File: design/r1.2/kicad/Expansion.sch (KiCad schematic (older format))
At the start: 27 parts, among them IC1 MC68010P10, IC4 MC68901P, IC6 74174N, IC9 74LS01N, J1 PWR, J3 Conn_02x32_Odd_Even, J5 GPIO-PANEL

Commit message: Layout for 1.2 and PLD changes for same
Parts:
- J5: symbol Connector_Generic:Conn_2Rows-15Pins -> Connector_Generic:Conn_02x08_Odd_Even
- renumbered C13 to C14, C14 to C15, C15 to C16, C16 to C17, C17 to C18, C23 to C19, C18 to C20, C25 to C21, C19 to C22, C20 to C23, C21 to C24, C22 to C25, C24 to C26, R15 to R17, R16 to R18, R17 to R19
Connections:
- net GND: now also J5.16 (Pin_16)
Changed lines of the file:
@@
 $EndComp
 $Comp
-L Connector_Generic:Conn_2Rows-15Pins J5
+L Connector_Generic:Conn_02x08_Odd_Even J5
 U 1 1 600521A7
 P 10250 7000
@@
 Text GLabel 10050 7400 0    50   Input ~ 0
 TAI
-Text GLabel 10550 7300 2    50   Input ~ 0
-TBI
 Text GLabel 11300 2800 2    50   Input ~ 0
 VPA
@@
 	10300 8100 10300 7950
 $Comp
-L Device:R R17
+L Device:R R19
 U 1 1 600B8632
 P 11100 2300
-F 0 "R17" H 11170 2346 50  0000 L CNN
+F 0 "R19" H 11170 2346 50  0000 L CNN
 F 1 "10K" H 11170 2255 50  0000 L CNN
 F 2 "rosco_m68k:0207_10" V 11030 2300 50  0001 C CNN
@@
 AR Path="/5F55DF35" Ref="C?"  Part="1"
 AR Path="/5E53B952/5F55DF35" Ref="C?"  Part="1"
-AR Path="/5E53BC83/5F55DF35" Ref="C25"  Part="1"
-F 0 "C25" H 3795 6569 59  0000 L BNN
+AR Path="/5E53BC83/5F55DF35" Ref="C21"  Part="1"
+F 0 "C21" H 3795 6569 59  0000 L BNN
 F 1 "470uF" H 3795 6369 59  0000 L BNN
 F 2 "rosco_m68k:E3,5-10" H 3750 6550 50  0001 C CNN
@@
 AR Path="/5F55DF3B" Ref="C?"  Part="1"
 AR Path="/5E53B952/5F55DF3B" Ref="C?"  Part="1"
-AR Path="/5E53BC83/5F55DF3B" Ref="C23"  Part="1"
-F 0 "C23" H 3295 6569 59  0000 L BNN
+AR Path="/5E53BC83/5F55DF3B" Ref="C19"  Part="1"
+F 0 "C19" H 3295 6569 59  0000 L BNN
 F 1 "100uF" H 3295 6369 59  0000 L BNN
 F 2 "rosco_m68k:E2,5-5" H 3250 6550 50  0001 C CNN
@@
 	11700 2700 11700 5550
 $Comp
-L Device:R R16
+L Device:R R18
 U 1 1 6009E518
 P 10550 7700
-F 0 "R16" H 10620 7746 50  0000 L CNN
+F 0 "R18" H 10620 7746 50  0000 L CNN
 F 1 "4K7" H 10620 7655 50  0000 L CNN
 F 2 "rosco_m68k:0207_10" V 10480 7700 50  0001 C CNN
@@
 $EndComp
 $Comp
-L Device:R R15
+L Device:R R17
 U 1 1 6009D68E
 P 10050 7700
-F 0 "R15" H 10120 7746 50  0000 L CNN
+F 0 "R17" H 10120 7746 50  0000 L CNN
 F 1 "4K7" H 10120 7655 50  0000 L CNN
 F 2 "rosco_m68k:0207_10" V 9980 7700 50  0001 C CNN
@@
 Wire Wire Line
 	10050 7400 10050 7550
-Wire Wire Line
-	10550 7300 10550 7550
 Wire Wire Line
 	10050 7850 10050 7950
@@
 AR Path="/5E53B630/5F6756E5" Ref="C?"  Part="1"
 AR Path="/5E53B4B8/5F6756E5" Ref="C?"  Part="1"
-AR Path="/5E53BC83/5F6756E5" Ref="C20"  Part="1"
-F 0 "C20" H 4660 8715 59  0000 L BNN
+AR Path="/5E53BC83/5F6756E5" Ref="C23"  Part="1"
+F 0 "C23" H 4660 8715 59  0000 L BNN
 F 1 "100nF" H 4660 8515 59  0000 L BNN
 F 2 "rosco_m68k:C2.5-3" H 4600 8700 50  0001 C CNN
@@
 AR Path="/5E53B630/5F6756EB" Ref="C?"  Part="1"
 AR Path="/5E53B4B8/5F6756EB" Ref="C?"  Part="1"
-AR Path="/5E53BC83/5F6756EB" Ref="C21"  Part="1"
-F 0 "C21" H 5510 8715 59  0000 L BNN
+AR Path="/5E53BC83/5F6756EB" Ref="C24"  Part="1"
+F 0 "C24" H 5510 8715 59  0000 L BNN
 F 1 "100nF" H 5510 8515 59  0000 L BNN
 F 2 "rosco_m68k:C2.5-3" H 5450 8700 50  0001 C CNN
@@
 AR Path="/5F699F50" Ref="C?"  Part="1"
 AR Path="/5E53B4B8/5F699F50" Ref="C?"  Part="1"
-AR Path="/5E53BC83/5F699F50" Ref="C18"  Part="1"
-F 0 "C18" H 3360 8715 59  0000 L BNN
+AR Path="/5E53BC83/5F699F50" Ref="C20"  Part="1"
+F 0 "C20" H 3360 8715 59  0000 L BNN
 F 1 "100nF" H 3360 8515 59  0000 L BNN
 F 2 "rosco_m68k:C2.5-3" H 3300 8700 50  0001 C CNN
@@
 AR Path="/5F699F56" Ref="C?"  Part="1"
 AR Path="/5E53B4B8/5F699F56" Ref="C?"  Part="1"
-AR Path="/5E53BC83/5F699F56" Ref="C19"  Part="1"
-F 0 "C19" H 4210 8715 59  0000 L BNN
+AR Path="/5E53BC83/5F699F56" Ref="C22"  Part="1"
+F 0 "C22" H 4210 8715 59  0000 L BNN
 F 1 "100nF" H 4210 8515 59  0000 L BNN
 F 2 "rosco_m68k:C2.5-3" H 4150 8700 50  0001 C CNN
@@
 AR Path="/5F699F5C" Ref="C?"  Part="1"
 AR Path="/5E53B4B8/5F699F5C" Ref="C?"  Part="1"
-AR Path="/5E53BC83/5F699F5C" Ref="C13"  Part="1"
-F 0 "C13" H 1195 8719 59  0000 L BNN
+AR Path="/5E53BC83/5F699F5C" Ref="C14"  Part="1"
+F 0 "C14" H 1195 8719 59  0000 L BNN
 F 1 "100uF" H 1195 8519 59  0000 L BNN
 F 2 "rosco_m68k:E2,5-5" H 1150 8700 50  0001 C CNN
@@
 AR Path="/5F699F62" Ref="C?"  Part="1"
 AR Path="/5E53B4B8/5F699F62" Ref="C?"  Part="1"
-AR Path="/5E53BC83/5F699F62" Ref="C17"  Part="1"
-F 0 "C17" H 2895 8719 59  0000 L BNN
+AR Path="/5E53BC83/5F699F62" Ref="C18"  Part="1"
+F 0 "C18" H 2895 8719 59  0000 L BNN
 F 1 "100uF" H 2895 8519 59  0000 L BNN
 F 2 "rosco_m68k:E2,5-5" H 2850 8700 50  0001 C CNN
@@
 AR Path="/5F6CD656" Ref="C?"  Part="1"
 AR Path="/5E53B952/5F6CD656" Ref="C?"  Part="1"
-AR Path="/5E53BC83/5F6CD656" Ref="C24"  Part="1"
-F 0 "C24" H 6760 8715 59  0000 L BNN
+AR Path="/5E53BC83/5F6CD656" Ref="C26"  Part="1"
+F 0 "C26" H 6760 8715 59  0000 L BNN
 F 1 "100nF" H 6760 8515 59  0000 L BNN
 F 2 "rosco_m68k:C2.5-3" H 6700 8700 50  0001 C CNN
@@
 AR Path="/5E53B810/5F6CD66A" Ref="C?"  Part="1"
 AR Path="/5E53B952/5F6CD66A" Ref="C?"  Part="1"
-AR Path="/5E53BC83/5F6CD66A" Ref="C22"  Part="1"
-F 0 "C22" H 5960 8715 59  0000 L BNN
+AR Path="/5E53BC83/5F6CD66A" Ref="C25"  Part="1"
+F 0 "C25" H 5960 8715 59  0000 L BNN
 F 1 "100nF" H 5960 8515 59  0000 L BNN
 F 2 "rosco_m68k:C2.5-3" H 5900 8700 50  0001 C CNN
@@
 AR Path="/5E53B810/5F6CD670" Ref="C?"  Part="1"
 AR Path="/5E53B952/5F6CD670" Ref="C?"  Part="1"
-AR Path="/5E53BC83/5F6CD670" Ref="C14"  Part="1"
-F 0 "C14" H 1595 8719 59  0000 L BNN
+AR Path="/5E53BC83/5F6CD670" Ref="C15"  Part="1"
+F 0 "C15" H 1595 8719 59  0000 L BNN
 F 1 "100uF" H 1595 8519 59  0000 L BNN
 F 2 "rosco_m68k:E2,5-5" H 1550 8700 50  0001 C CNN
@@
 AR Path="/5E53B810/5F6CD676" Ref="C?"  Part="1"
 AR Path="/5E53B952/5F6CD676" Ref="C?"  Part="1"
-AR Path="/5E53BC83/5F6CD676" Ref="C16"  Part="1"
-F 0 "C16" H 2495 8719 59  0000 L BNN
+AR Path="/5E53BC83/5F6CD676" Ref="C17"  Part="1"
+F 0 "C17" H 2495 8719 59  0000 L BNN
 F 1 "100uF" H 2495 8519 59  0000 L BNN
 F 2 "rosco_m68k:E2,5-5" H 2450 8700 50  0001 C CNN
@@
 AR Path="/5E53B810/5F6CD67C" Ref="C?"  Part="1"
 AR Path="/5E53B952/5F6CD67C" Ref="C?"  Part="1"
-AR Path="/5E53BC83/5F6CD67C" Ref="C15"  Part="1"
-F 0 "C15" H 2045 8719 59  0000 L BNN
+AR Path="/5E53BC83/5F6CD67C" Ref="C16"  Part="1"
+F 0 "C16" H 2045 8719 59  0000 L BNN
 F 1 "100uF" H 2045 8519 59  0000 L BNN
 F 2 "rosco_m68k:E2,5-5" H 2000 8700 50  0001 C CNN
@@
 	1150 7850 1150 8200
 Connection ~ 1150 8200
+Text GLabel 10550 7400 2    50   UnSpc ~ 0
+GND
+Wire Wire Line
+	10550 7300 10750 7300
+Wire Wire Line
+	10750 7300 10750 7550
+Wire Wire Line
+	10750 7550 10550 7550
+Wire Wire Line
+	10750 7300 10850 7300
 Wire Bus Line
 	11150 4100 11150 5700
 Wire Bus Line
 	9450 2150 9450 4500
+Connection ~ 10750 7300
+Text GLabel 10850 7300 2    50   Input ~ 0
+TBI
 $EndSCHEMATC

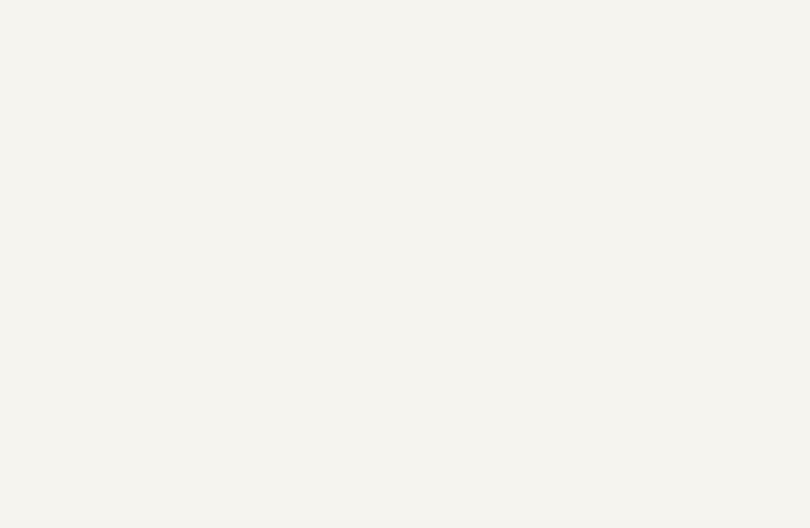
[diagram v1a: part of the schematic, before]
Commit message: Fix reset LED snafu
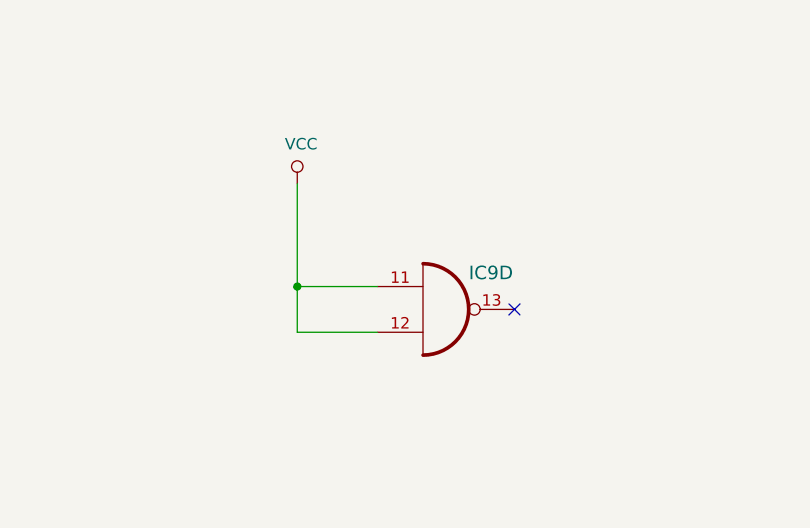
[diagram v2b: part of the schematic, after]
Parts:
- added unit 4 of IC9
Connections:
- net VCC: now also IC9.11 (I0), IC9.12 (I1)
- no-connect marks 0 -> 1
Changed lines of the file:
@@
 Wire Wire Line
 	10750 7300 10850 7300
+Connection ~ 10750 7300
+Text GLabel 10850 7300 2    50   Input ~ 0
+TBI
+$Comp
+L rosco_m68k-eagle-import:7401N IC?
+U 4 1 5F01DA9B
+P 3550 2950
+AR Path="/5F01DA9B" Ref="IC?"  Part="3"
+AR Path="/5E53B952/5F01DA9B" Ref="IC?"  Part="4"
+AR Path="/5E53BC83/5F01DA9B" Ref="IC9"  Part="4"
+F 0 "IC9" H 3650 3075 59  0000 L BNN
+F 1 "74LS01N" H 3650 2750 59  0001 L BNN
+F 2 "rosco_m68k:DIL14" H 3550 2950 50  0001 C CNN
+F 3 "" H 3550 2950 50  0001 C CNN
+	4    3550 2950
+	1    0    0    -1
+$EndComp
+NoConn ~ 3850 2950
+Wire Wire Line
+	2900 2400 2900 2850
+Wire Wire Line
+	2900 3050 3250 3050
+Wire Wire Line
+	3250 2850 2900 2850
 Wire Bus Line
 	11150 4100 11150 5700
 Wire Bus Line
 	9450 2150 9450 4500
-Connection ~ 10750 7300
-Text GLabel 10850 7300 2    50   Input ~ 0
-TBI
+Connection ~ 2900 2850
+Wire Wire Line
+	2900 2850 2900 3050
+$Comp
+L power:VCC #PWR?
+U 1 1 5F03938E
+P 2900 2400
+F 0 "#PWR?" H 2900 2250 50  0001 C CNN
+F 1 "VCC" H 2917 2573 50  0000 C CNN
+F 2 "" H 2900 2400 50  0001 C CNN
+F 3 "" H 2900 2400 50  0001 C CNN
+	1    2900 2400
+	1    0    0    -1
+$EndComp
 $EndSCHEMATC

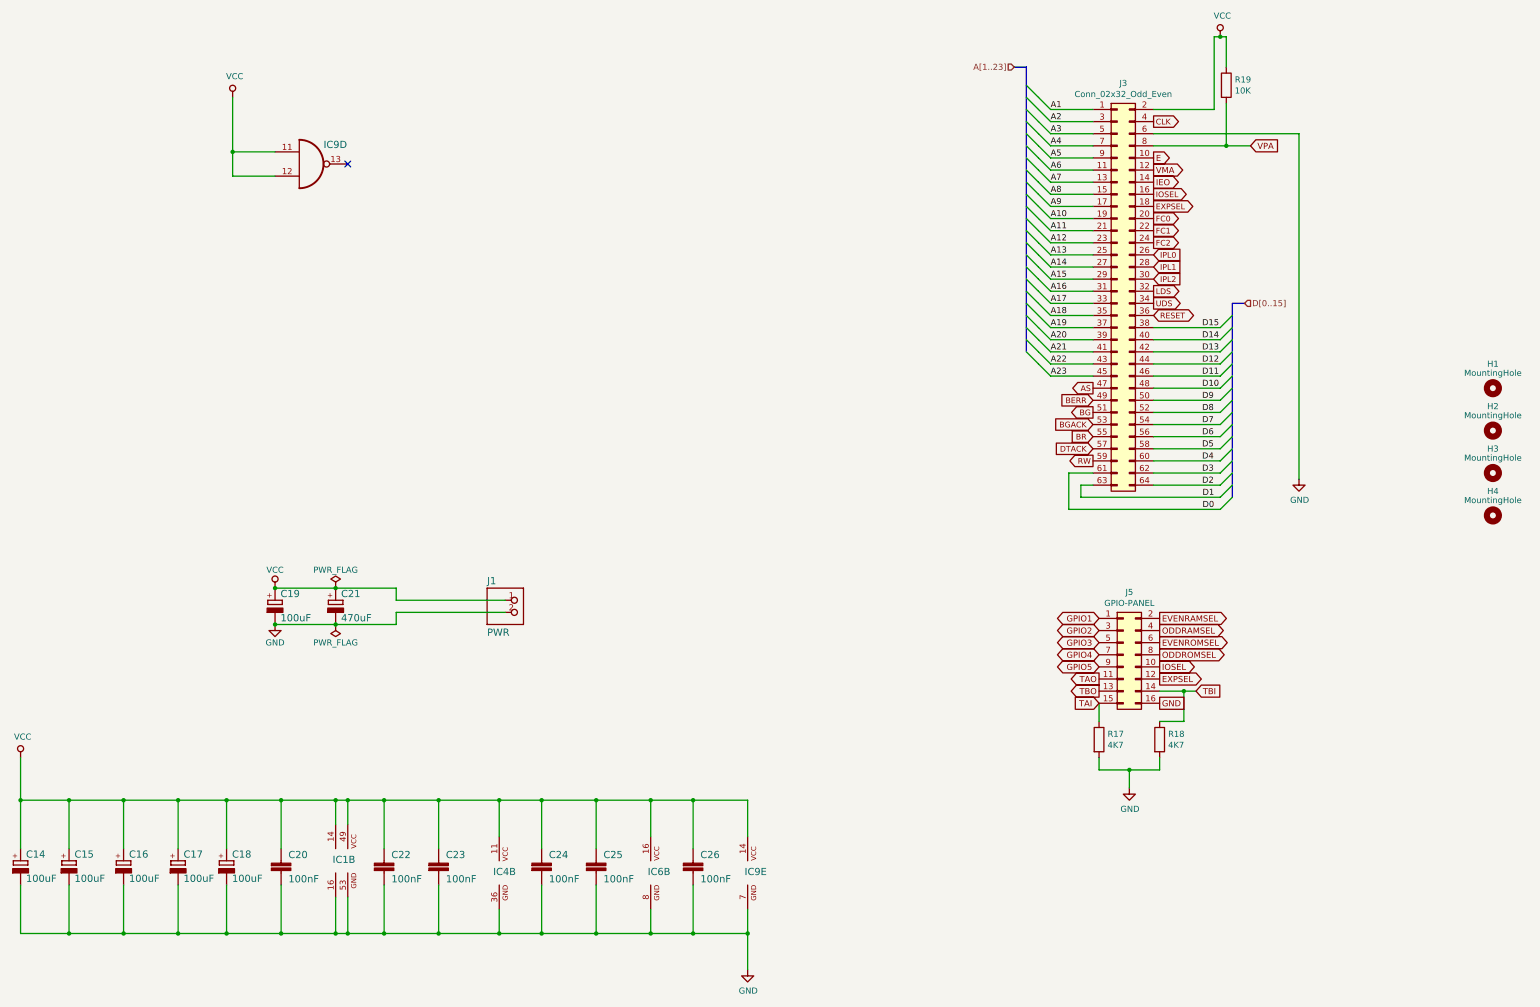
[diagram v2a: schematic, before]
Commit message: Add DTACK watchdog, tidy up footprints
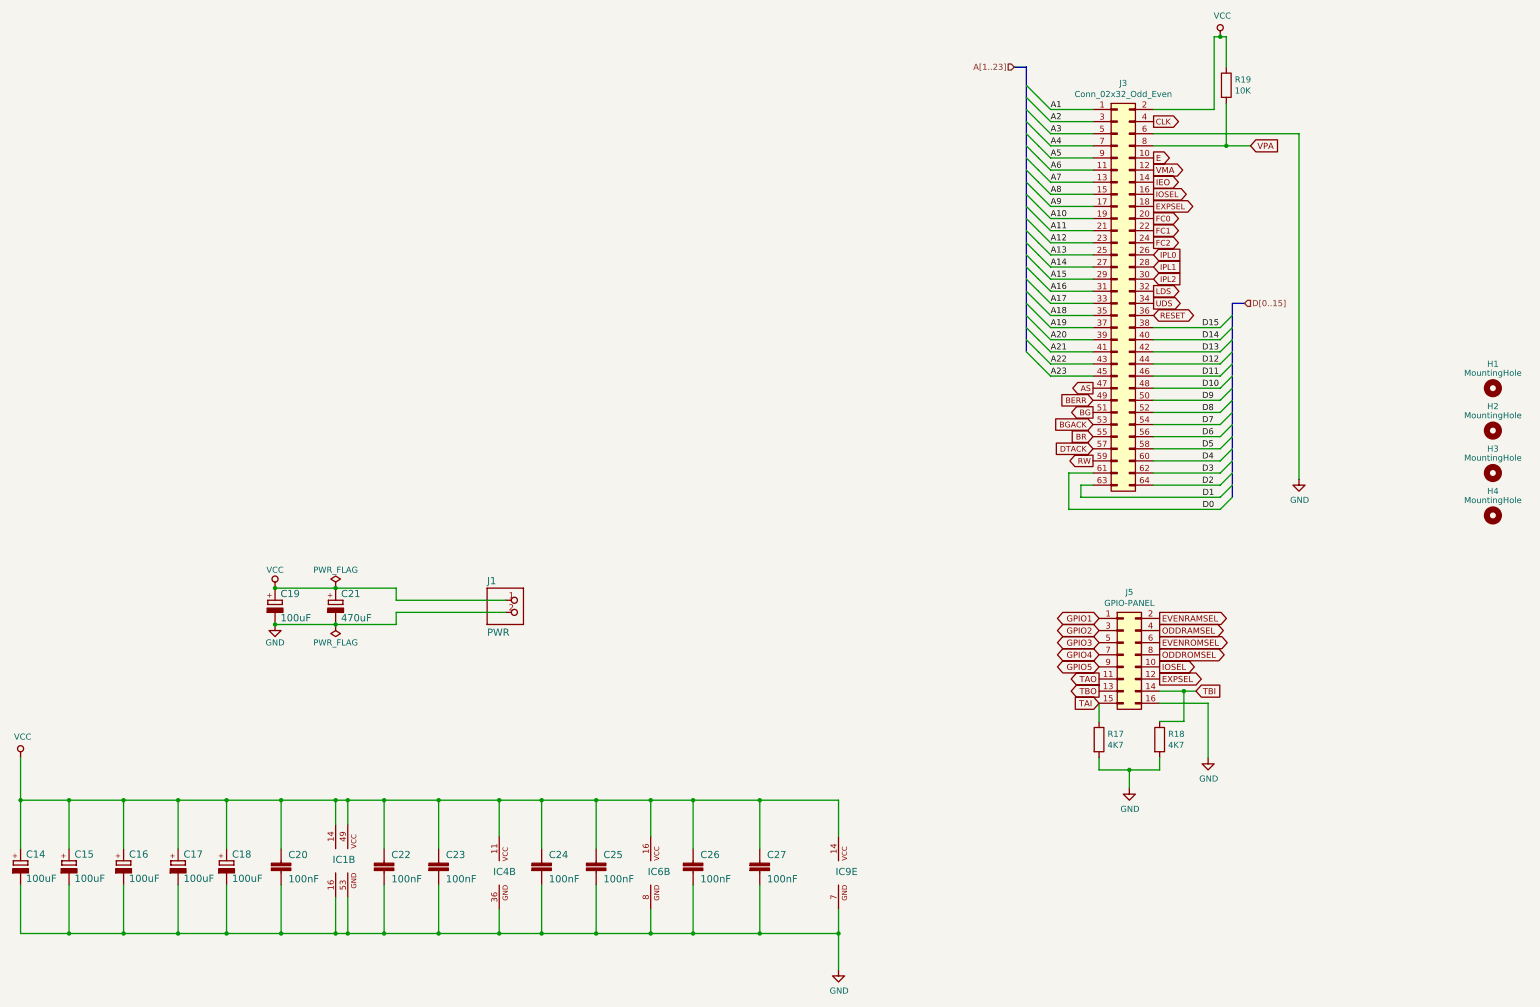
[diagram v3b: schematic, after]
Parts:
- removed unit 4 of IC9
- added C27: 100nF, rosco_m68k:C2.5-3, symbol rosco_m68k-eagle-import:C2,5-3
- IC6: footprint rosco_m68k:DIL16 -> Package_DIP:DIP-16_W7.62mm_Socket_LongPads
- IC9: footprint rosco_m68k:DIL14 -> Package_DIP:DIP-14_W7.62mm_Socket_LongPads
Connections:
- net GND: now also C27.2
- net VCC: now also C27.1
- no-connect marks 1 -> 0
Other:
- moved on the sheet: IC9E
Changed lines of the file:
@@
 L rosco_m68k-eagle-import:7401N IC?
 U 5 1 5F6CD650
-P 7150 8800
+P 7900 8800
 AR Path="/5F6CD650" Ref="IC?"  Part="5"
 AR Path="/5E53B952/5F6CD650" Ref="IC?"  Part="5"
 AR Path="/5E53BC83/5F6CD650" Ref="IC9"  Part="5"
-F 0 "IC9" H 7125 8775 59  0000 L BNN
-F 1 "74LS01N" H 7250 8600 59  0001 L BNN
-F 2 "rosco_m68k:DIL14" H 7150 8800 50  0001 C CNN
-F 3 "" H 7150 8800 50  0001 C CNN
-	5    7150 8800
+F 0 "IC9" H 7875 8775 59  0000 L BNN
+F 1 "74LS01N" H 8000 8600 59  0001 L BNN
+F 2 "Package_DIP:DIP-14_W7.62mm_Socket_LongPads" H 7900 8800 50  0001 C CNN
+F 3 "" H 7900 8800 50  0001 C CNN
+	5    7900 8800
 	1    0    0    -1
 $EndComp
@@
 F 0 "IC6" H 6325 8775 59  0000 L BNN
 F 1 "74174N" H 6050 8200 59  0001 L BNN
-F 2 "rosco_m68k:DIL16" H 6350 8800 50  0001 C CNN
+F 2 "Package_DIP:DIP-16_W7.62mm_Socket_LongPads" H 6350 8800 50  0001 C CNN
 F 3 "" H 6350 8800 50  0001 C CNN
 	2    6350 8800
@@
 	3850 9300 4150 9300
 Wire Wire Line
-	7150 9300 7150 9100
+	7900 9300 7900 9100
 Connection ~ 3850 9300
 Wire Wire Line
-	7150 8500 7150 8200
-Wire Wire Line
-	7150 8200 6700 8200
+	7900 8500 7900 8200
 Connection ~ 3850 8200
 Wire Wire Line
@@
 Wire Wire Line
 	6700 8600 6700 8200
-Connection ~ 6700 8200
 Wire Wire Line
 	6700 8200 6350 8200
 Wire Wire Line
 	6700 8900 6700 9300
-Connection ~ 6700 9300
-Wire Wire Line
-	6700 9300 7150 9300
 Wire Wire Line
 	6350 9100 6350 9300
@@
 L power:GND #PWR0109
 U 1 1 5F7D403D
-P 7150 9600
-F 0 "#PWR0109" H 7150 9350 50  0001 C CNN
-F 1 "GND" H 7155 9427 50  0000 C CNN
-F 2 "" H 7150 9600 50  0001 C CNN
-F 3 "" H 7150 9600 50  0001 C CNN
-	1    7150 9600
-	1    0    0    -1
-$EndComp
-Wire Wire Line
-	7150 9600 7150 9300
-Connection ~ 7150 9300
+P 7900 9600
+F 0 "#PWR0109" H 7900 9350 50  0001 C CNN
+F 1 "GND" H 7905 9427 50  0000 C CNN
+F 2 "" H 7900 9600 50  0001 C CNN
+F 3 "" H 7900 9600 50  0001 C CNN
+	1    7900 9600
+	1    0    0    -1
+$EndComp
+Wire Wire Line
+	7900 9600 7900 9300
+Connection ~ 7900 9300
 Wire Wire Line
 	1150 7850 1150 8200
 Connection ~ 1150 8200
-Text GLabel 10550 7400 2    50   UnSpc ~ 0
-GND
 Wire Wire Line
 	10550 7300 10750 7300
@@
 TBI
 $Comp
-L rosco_m68k-eagle-import:7401N IC?
-U 4 1 5F01DA9B
-P 3550 2950
-AR Path="/5F01DA9B" Ref="IC?"  Part="3"
-AR Path="/5E53B952/5F01DA9B" Ref="IC?"  Part="4"
-AR Path="/5E53BC83/5F01DA9B" Ref="IC9"  Part="4"
-F 0 "IC9" H 3650 3075 59  0000 L BNN
-F 1 "74LS01N" H 3650 2750 59  0001 L BNN
-F 2 "rosco_m68k:DIL14" H 3550 2950 50  0001 C CNN
-F 3 "" H 3550 2950 50  0001 C CNN
-	4    3550 2950
-	1    0    0    -1
-$EndComp
-NoConn ~ 3850 2950
-Wire Wire Line
-	2900 2400 2900 2850
-Wire Wire Line
-	2900 3050 3250 3050
-Wire Wire Line
-	3250 2850 2900 2850
+L rosco_m68k-eagle-import:C2,5-3 C?
+U 1 1 5F3EE222
+P 7250 8700
+AR Path="/5F3EE222" Ref="C?"  Part="1"
+AR Path="/5E53B810/5F3EE222" Ref="C?"  Part="1"
+AR Path="/5E53B952/5F3EE222" Ref="C?"  Part="1"
+AR Path="/5E53BC83/5F3EE222" Ref="C27"  Part="1"
+F 0 "C27" H 7310 8715 59  0000 L BNN
+F 1 "100nF" H 7310 8515 59  0000 L BNN
+F 2 "rosco_m68k:C2.5-3" H 7250 8700 50  0001 C CNN
+F 3 "" H 7250 8700 50  0001 C CNN
+	1    7250 8700
+	1    0    0    -1
+$EndComp
+Wire Wire Line
+	7250 8600 7250 8200
+Wire Wire Line
+	6700 8200 7250 8200
+Connection ~ 6700 8200
+Wire Wire Line
+	7250 8200 7900 8200
+Connection ~ 7250 8200
+Wire Wire Line
+	7250 8900 7250 9300
+Wire Wire Line
+	7250 9300 7900 9300
+Wire Wire Line
+	7250 9300 6700 9300
+Connection ~ 7250 9300
+Connection ~ 6700 9300
+$Comp
+L power:GND #PWR0113
+U 1 1 5F499969
+P 10950 7850
+F 0 "#PWR0113" H 10950 7600 50  0001 C CNN
+F 1 "GND" H 10955 7677 50  0000 C CNN
+F 2 "" H 10950 7850 50  0001 C CNN
+F 3 "" H 10950 7850 50  0001 C CNN
+	1    10950 7850
+	1    0    0    -1
+$EndComp
+Wire Wire Line
+	10550 7400 10950 7400
+Wire Wire Line
+	10950 7400 10950 7850
 Wire Bus Line
 	11150 4100 11150 5700
 Wire Bus Line
 	9450 2150 9450 4500
-Connection ~ 2900 2850
-Wire Wire Line
-	2900 2850 2900 3050
-$Comp
-L power:VCC #PWR?
-U 1 1 5F03938E
-P 2900 2400
-F 0 "#PWR?" H 2900 2250 50  0001 C CNN
-F 1 "VCC" H 2917 2573 50  0000 C CNN
-F 2 "" H 2900 2400 50  0001 C CNN
-F 3 "" H 2900 2400 50  0001 C CNN
-	1    2900 2400
-	1    0    0    -1
-$EndComp
 $EndSCHEMATC
